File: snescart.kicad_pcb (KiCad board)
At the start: 2 copper layers, 101.6 x 37.3 mm, 7 parts, among them P1 CASSETTE, U1 27C080

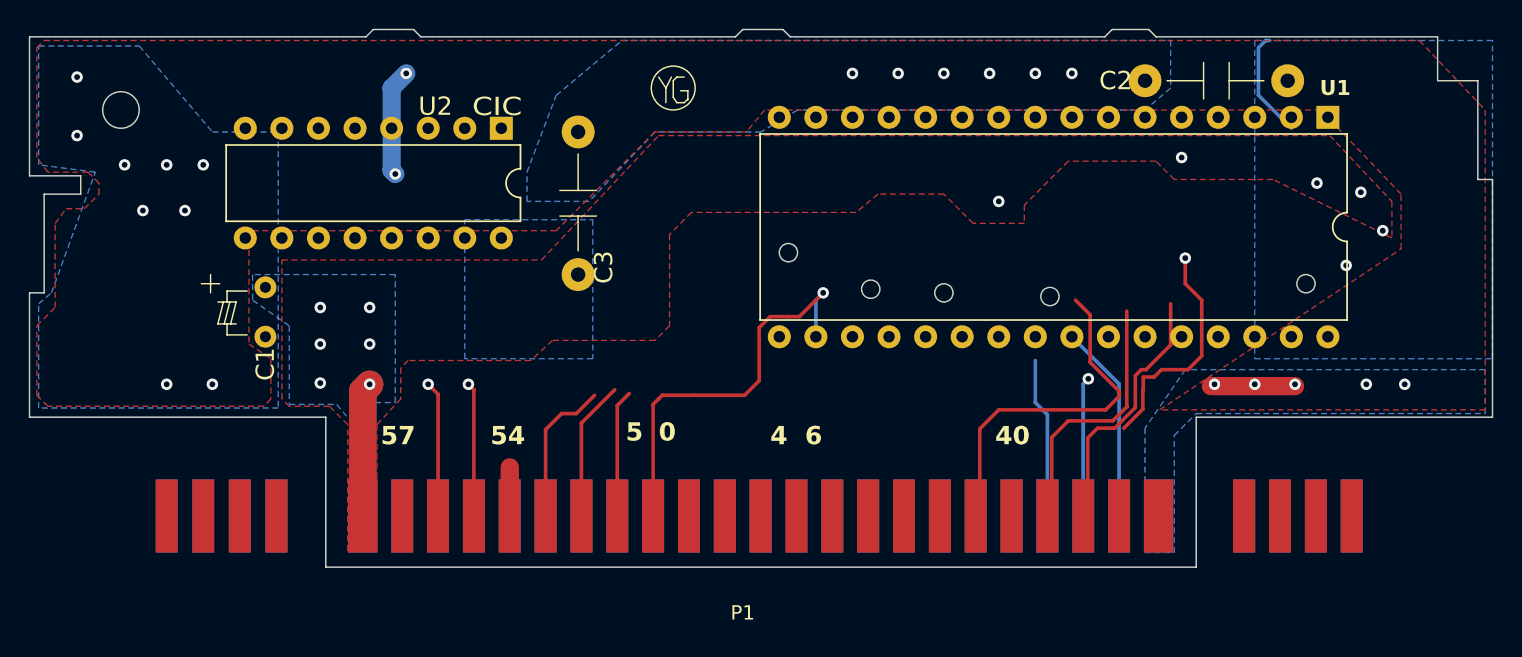
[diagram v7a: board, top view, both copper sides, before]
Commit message: power trace was gone again
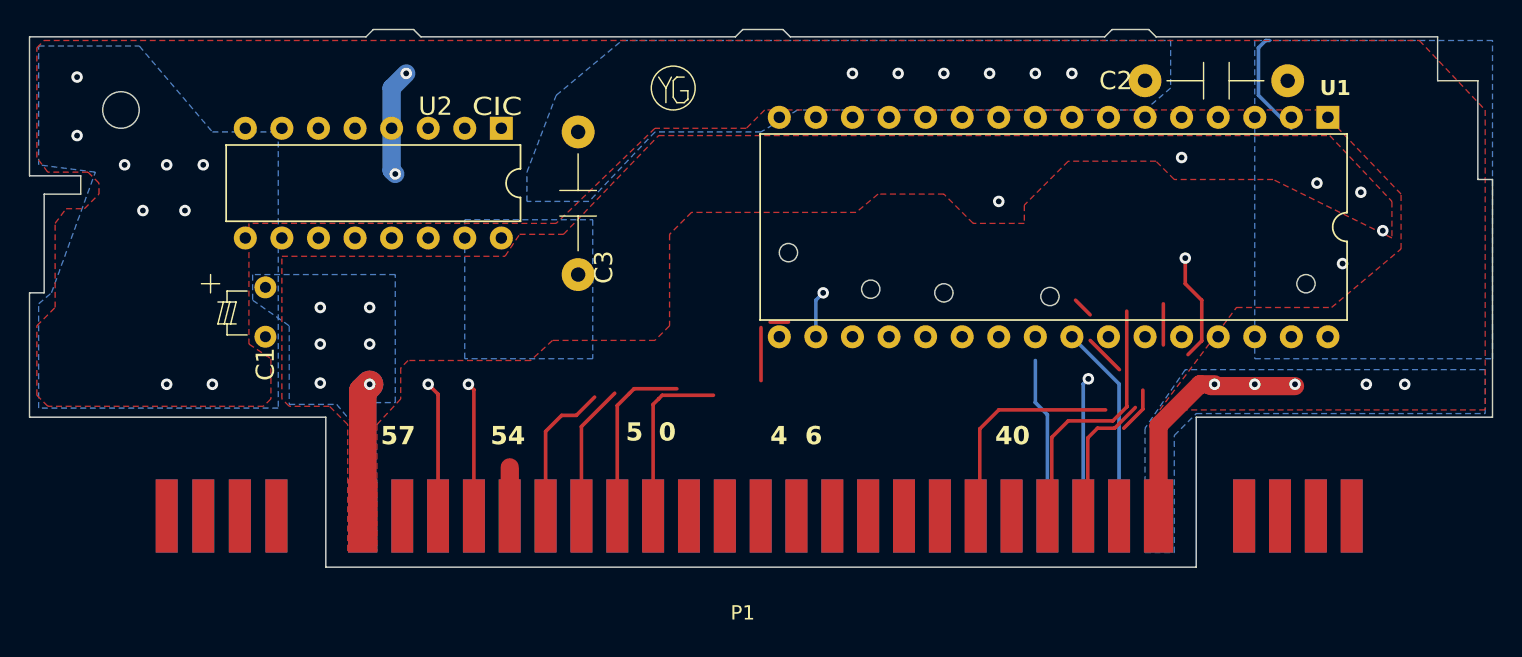
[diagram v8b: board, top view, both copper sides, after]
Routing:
- net GND: track 13.4 -> 24.7 mm
- net Net-(P1-D4): track 28.2 -> 20.4 mm
- net Net-(P1-A13): track 18.4 -> 12.8 mm
- net Net-(P1-A12): track 16.1 -> 10.8 mm
- net Net-(P1-A16): track 32.5 -> 27.5 mm
- net Net-(P1-D5): track 8.86 -> 12.3 mm
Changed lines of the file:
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@@
       (pts (xy 170.4086 148.3106) (xy 171.3738 148.3106))
       (height 5.08)
-      (gr_text "0.0380 in" (at 170.8912 152.2906) (layer "User.2")
+      (gr_text "0.9652 mm" (at 170.8912 152.2906) (layer "User.2")
         (effects (font (size 1 1) (thickness 0.1)))
       )
@@
       (pts (xy 120.1166 143.891) (xy 169.6466 143.891))
       (height -5.207)
-      (gr_text "1.9500 in" (at 143.4846 136.144) (layer "User.2")
+      (gr_text "49.5300 mm" (at 143.4846 136.144) (layer "User.2")
         (effects (font (size 1 1) (thickness 0.1)))
       )
@@
     (effects (font (size 1.5 1.5) (thickness 0.3) bold) (justify left bottom))
   )
+  (segment (start 172.3898 140.0302) (end 175.26 137.16) (width 1.27) (layer "F.Cu") (net 1))
+  (segment (start 172.3898 146.304) (end 172.3898 140.0302) (width 1.27) (layer "F.Cu") (net 1))
+  (segment (start 175.26 137.16) (end 176.276 137.16) (width 1.27) (layer "F.Cu") (net 1))
   (segment (start 176.022 137.287) (end 181.864 137.287) (width 1.27) (layer "F.Cu") (net 1))
   (via (at 97.282 115.824) (size 0.8) (drill 0.4) (layers "F.Cu" "B.Cu") (free) (net 1))
@@
   (segment (start 124.841 146.304) (end 124.841 137.541) (width 0.254) (layer "F.Cu") (net 25))
   (via (at 124.46 137.16) (size 0.8) (drill 0.4) (layers "F.Cu" "B.Cu") (net 25))
-  (segment (start 172.593 136.144) (end 172.085 136.652) (width 0.25) (layer "F.Cu") (net 35))
+  (segment (start 175.387 131.318) (end 175.387 134.142995) (width 0.25) (layer "F.Cu") (net 35))
   (segment (start 174.244 130.175) (end 175.387 131.318) (width 0.25) (layer "F.Cu") (net 35))
-  (segment (start 171.2976 137.5664) (end 171.323 137.541) (width 0.254) (layer "F.Cu") (net 35))
   (segment (start 169.975 140.2098) (end 171.2976 138.8872) (width 0.254) (layer "F.Cu") (net 35))
   (segment (start 174.244 128.397) (end 174.244 130.175) (width 0.25) (layer "F.Cu") (net 35))
-  (segment (start 172.085 136.652) (end 171.323 136.652) (width 0.25) (layer "F.Cu") (net 35))
-  (segment (start 175.387 135.189991) (end 174.432991 136.144) (width 0.25) (layer "F.Cu") (net 35))
-  (segment (start 175.387 131.318) (end 175.387 135.189991) (width 0.25) (layer "F.Cu") (net 35))
-  (segment (start 174.432991 136.144) (end 172.593 136.144) (width 0.25) (layer "F.Cu") (net 35))
+  (segment (start 175.387 134.142995) (end 174.432991 135.097004) (width 0.25) (layer "F.Cu") (net 35))
   (segment (start 171.2976 138.8872) (end 171.2976 137.5664) (width 0.254) (layer "F.Cu") (net 35))
-  (segment (start 171.323 137.541) (end 171.323 136.652) (width 0.254) (layer "F.Cu") (net 35))
   (via (at 174.244 128.397) (size 0.8) (drill 0.4) (layers "F.Cu" "B.Cu") (net 35))
   (segment (start 167.475 146.685) (end 167.475 140.881) (width 0.25) (layer "F.Cu") (net 36))
-  (segment (start 173.228 134.427991) (end 173.228 131.572) (width 0.25) (layer "F.Cu") (net 36))
-  (segment (start 170.774788 136.560987) (end 171.191775 136.144) (width 0.25) (layer "F.Cu") (net 36))
-  (segment (start 171.511991 136.144) (end 173.228 134.427991) (width 0.25) (layer "F.Cu") (net 36))
+  (segment (start 172.72 134.427991) (end 172.72 131.572) (width 0.25) (layer "F.Cu") (net 36))
   (segment (start 167.475 140.881) (end 168.148 140.208) (width 0.25) (layer "F.Cu") (net 36))
-  (segment (start 171.191775 136.144) (end 171.511991 136.144) (width 0.25) (layer "F.Cu") (net 36))
   (segment (start 169.337576 140.208) (end 170.774788 138.770788) (width 0.25) (layer "F.Cu") (net 36))
-  (segment (start 170.774788 138.770788) (end 170.774788 136.560987) (width 0.25) (layer "F.Cu") (net 36))
   (segment (start 168.148 140.208) (end 169.337576 140.208) (width 0.25) (layer "F.Cu") (net 36))
   (segment (start 164.975 146.685) (end 164.975 140.841) (width 0.25) (layer "F.Cu") (net 37))
@@
   (segment (start 159.975 140.253) (end 161.29 138.938) (width 0.25) (layer "F.Cu") (net 39))
   (segment (start 167.64 132.334) (end 166.624 131.318) (width 0.25) (layer "F.Cu") (net 39))
-  (segment (start 167.64 135.636) (end 167.64 132.334) (width 0.25) (layer "F.Cu") (net 39))
-  (segment (start 169.672 137.98) (end 169.672 137.668) (width 0.25) (layer "F.Cu") (net 39))
-  (segment (start 169.672 137.668) (end 167.64 135.636) (width 0.25) (layer "F.Cu") (net 39))
+  (segment (start 169.672 136.144) (end 167.64 134.112) (width 0.25) (layer "F.Cu") (net 39))
   (segment (start 161.29 138.938) (end 168.714 138.938) (width 0.25) (layer "F.Cu") (net 39))
-  (segment (start 168.714 138.938) (end 169.672 137.98) (width 0.25) (layer "F.Cu") (net 39))
   (segment (start 179.324 113.792) (end 179.832 113.284) (width 0.25) (layer "B.Cu") (net 39))
   (segment (start 181.61 119.375) (end 179.324 117.089) (width 0.25) (layer "B.Cu") (net 39))
   (segment (start 179.832 113.284) (end 180.086 113.284) (width 0.25) (layer "B.Cu") (net 39))
   (segment (start 179.324 117.089) (end 179.324 113.792) (width 0.25) (layer "B.Cu") (net 39))
-  (via (at 185.42 128.905) (size 0.8) (drill 0.4) (layers "F.Cu" "B.Cu") (net 42))
-  (segment (start 146.685 132.461) (end 147.447 132.461) (width 0.25) (layer "F.Cu") (net 48))
-  (segment (start 144.653 133.223) (end 145.415 132.461) (width 0.25) (layer "F.Cu") (net 48))
+  (via (at 185.166 128.778) (size 0.8) (drill 0.4) (layers "F.Cu" "B.Cu") (net 42))
   (segment (start 137.287 138.557) (end 137.668 138.176) (width 0.25) (layer "F.Cu") (net 48))
+  (segment (start 137.922 137.922) (end 141.478 137.922) (width 0.25) (layer "F.Cu") (net 48))
   (segment (start 137.668 138.176) (end 137.922 137.922) (width 0.25) (layer "F.Cu") (net 48))
-  (segment (start 144.653 136.906) (end 144.653 133.223) (width 0.25) (layer "F.Cu") (net 48))
-  (segment (start 137.922 137.922) (end 140.081 137.922) (width 0.25) (layer "F.Cu") (net 48))
-  (segment (start 140.081 137.922) (end 143.637 137.922) (width 0.25) (layer "F.Cu") (net 48))
-  (segment (start 143.637 137.922) (end 144.653 136.906) (width 0.25) (layer "F.Cu") (net 48))
-  (segment (start 145.415 132.461) (end 146.685 132.461) (width 0.25) (layer "F.Cu") (net 48))
-  (segment (start 147.447 132.461) (end 149.098 130.81) (width 0.25) (layer "F.Cu") (net 48))
+  (segment (start 144.78 136.906) (end 144.78 133.223) (width 0.25) (layer "F.Cu") (net 48))
+  (segment (start 145.415 132.842) (end 146.685 132.842) (width 0.25) (layer "F.Cu") (net 48))
   (segment (start 137.287 146.304) (end 137.287 138.557) (width 0.25) (layer "F.Cu") (net 48))
   (via (at 149.098 130.81) (size 0.8) (drill 0.4) (layers "F.Cu" "B.Cu") (net 48))
@@
   (segment (start 149.098 130.81) (end 148.59 131.318) (width 0.25) (layer "B.Cu") (net 48))
   (segment (start 134.7978 146.304) (end 134.7978 138.6332) (width 0.254) (layer "F.Cu") (net 49))
+  (segment (start 135.961 137.47) (end 138.938 137.47) (width 0.254) (layer "F.Cu") (net 49))
+  (segment (start 135.636 137.795) (end 135.961 137.47) (width 0.254) (layer "F.Cu") (net 49))
   (segment (start 134.7978 138.6332) (end 135.636 137.795) (width 0.254) (layer "F.Cu") (net 49))
   (segment (start 127.3302 146.304) (end 127.3302 142.9258) (width 1.27) (layer "F.Cu") (net 50))
-  (segment (start 132.3086 146.304) (end 132.3086 139.8524) (width 0.254) (layer "F.Cu") (net 52))
-  (segment (start 132.3086 139.8524) (end 134.62 137.541) (width 0.254) (layer "F.Cu") (net 52))
-  (segment (start 130.937 139.192) (end 131.953 139.192) (width 0.254) (layer "F.Cu") (net 53))
-  (segment (start 129.8194 140.3096) (end 130.937 139.192) (width 0.254) (layer "F.Cu") (net 53))
-  (segment (start 129.8194 146.304) (end 129.8194 140.3096) (width 0.254) (layer "F.Cu") (net 53))
-  (segment (start 131.953 139.192) (end 133.223 137.922) (width 0.254) (layer "F.Cu") (net 53))
+  (segment (start 132.3086 140.0937) (end 132.3086 146.304) (width 0.254) (layer "F.Cu") (net 52))
+  (segment (start 132.3086 140.0937) (end 134.62 137.7823) (width 0.254) (layer "F.Cu") (net 52))
+  (segment (start 130.937 139.319) (end 131.953 139.319) (width 0.254) (layer "F.Cu") (net 53))
+  (segment (start 129.8194 140.4366) (end 130.937 139.319) (width 0.254) (layer "F.Cu") (net 53))
+  (segment (start 129.8194 140.4366) (end 129.8194 146.304) (width 0.254) (layer "F.Cu") (net 53))
+  (segment (start 131.953 139.319) (end 133.223 138.049) (width 0.254) (layer "F.Cu") (net 53))
   (zone (net 2) (net_name "VCC") (layer "F.Cu") (hatch edge 0.5)
     (priority 2)
@@
         (xy 112.014 138.684)
         (xy 111.506 138.176)
-        (xy 111.506 128.524)
-        (xy 129.54 128.524)
+        (xy 111.506 128.27)
+        (xy 127 128.27)
+        (xy 128.016 126.746)
+        (xy 131.064 126.746)
         (xy 137.668 119.888)
         (xy 184.277 119.888)
@@
         (xy 195.072 138.938)
         (xy 172.466 138.938)
+        (xy 177.8 131.826)
+        (xy 184.404 131.826)
         (xy 189.23 127.762)
         (xy 189.23 123.952)
         (xy 183.642 118.11)
         (xy 145.034 118.11)
-        (xy 143.764 119.634)
-        (xy 137.414 119.634)
-        (xy 130.556 126.492)
-        (xy 109.22 126.492)
+        (xy 143.764 119.38)
+        (xy 137.414 119.38)
+        (xy 130.556 125.984)
+        (xy 109.22 125.984)
         (xy 109.22 134.366)
         (xy 110.744 135.382)
